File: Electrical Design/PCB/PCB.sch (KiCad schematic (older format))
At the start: 52 parts, among them J1 Conn_02x03_Odd_Even, J2 10118193-0001LF, M1 Camera_Servo, M2 Release_Servo, Q1 LED_MOS, Q2 CAMERA_MOS, Q3 RELEASE_MOS, U1 ADP3338AKCZ-5-R7, U2 BNO080, U3 ADP3338AKCZ-3.3-R7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

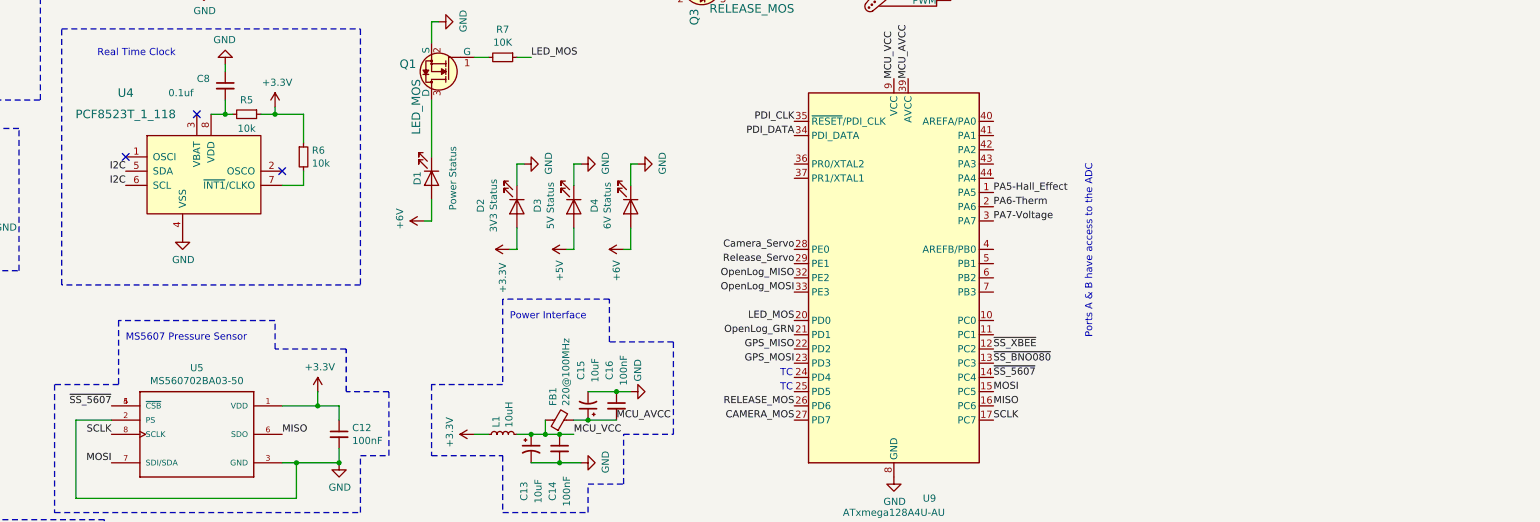
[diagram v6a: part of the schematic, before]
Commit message: Add a lot of libraries and footprints
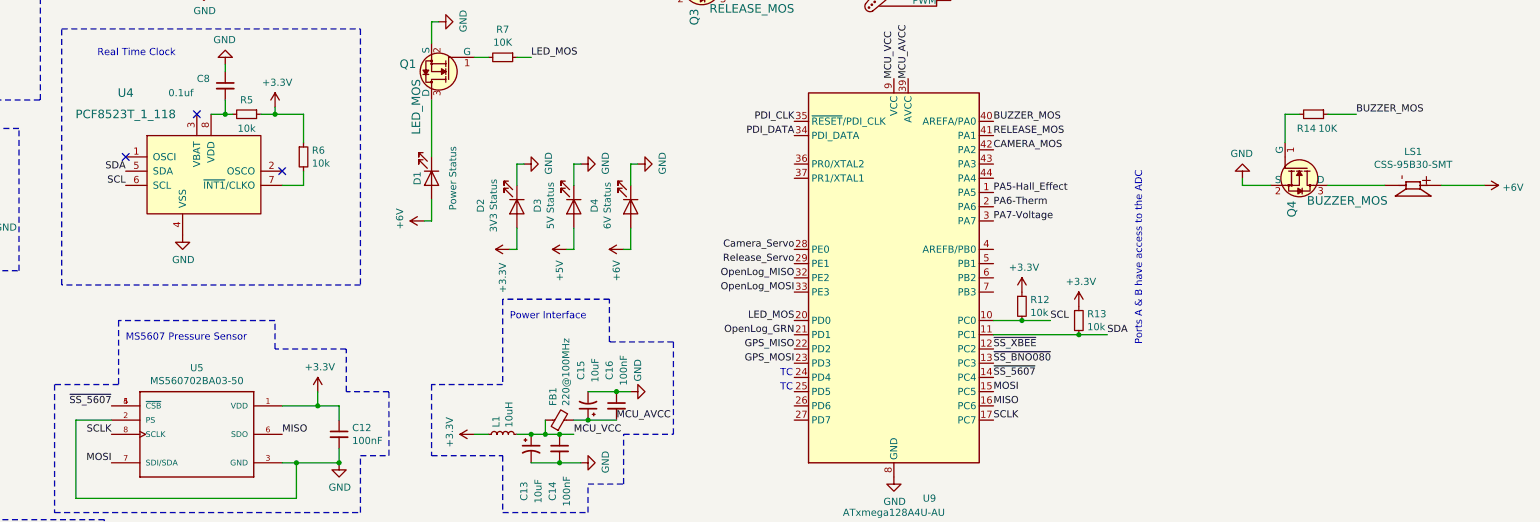
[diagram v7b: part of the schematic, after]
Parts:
- added LS1: CSS-95B30-SMT, CSS-95B30-SMT:CUI_CSS-95B30-SMT, symbol CSS-95B30-SMT:CSS-95B30-SMT
- added Q4: BUZZER_MOS, digikey-footprints:SOT-23-3, symbol dk_Transistors-FETs-MOSFETs-Single:2N7002K-T1-E3
- added R12, R13: 10k, Resistor_SMD:R_0805_2012Metric_Pad1.15x1.40mm_HandSolder, symbol Device:R_Small
- added R14: 10K, Resistor_SMD:R_0805_2012Metric_Pad1.15x1.40mm_HandSolder, symbol Device:R_Small
- J1: footprint (none) -> Connector:Tag-Connect_TC2030-IDC-FP_2x03_P1.27mm_Vertical
- M1, M2: footprint (none) -> Connector_PinHeader_2.54mm:PinHeader_1x03_P2.54mm_Horizontal
- R1, R10, R11, R2, R3, R4, R5, R6, R7, R8, R9: footprint Resistor_SMD:R_0805_2012Metric -> Resistor_SMD:R_0805_2012Metric_Pad1.15x1.40mm_HandSolder
- U1: footprint (none) -> ADP3338AKCZ-5-R7:SOT230P700X180-4N
- U2: footprint (none) -> BNO080:LGA-28
- U3: footprint (none) -> ADP3338AKCZ-3.3RL7:SOT230P700X180-4N
- U5: footprint (none) -> MS560702BA03-50:SON125P300X500X100-8N
- U6: footprint (none) -> Connector_PinHeader_2.00mm:PinHeader_1x03_P2.00mm_Horizontal
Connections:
- net +3V3: now also R12.1, R13.1
- net +6V: now also LS1.P
- net CAMERA_MOS: now also U9.42 (PA2); no longer U9.27 (PD7)
- net GND: now also Q4.2 (S)
- net RELEASE_MOS: now also U9.41 (PA1); no longer U9.26 (PD6)
- net SCL: now reaches U9.10 (PC0)
- net SCL: now also U4.6 (SCL), R12.2
- net SDA: now reaches U9.11 (PC1)
- net SDA: now also U4.5 (SDA), R13.2
- net BUZZER_MOS: now reaches U9.40 (AREFA/PA0)
- net BUZZER_MOS: now also R14.1
- removed net I2C: U4.5 (SDA), U4.6 (SCL)
- new net: LS1.N, Q4.3 (D)
- new net: Q4.1 (G), R14.2

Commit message: Netlist
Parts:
- C13, C15: footprint (none) -> Capacitor_THT:CP_Radial_D10.0mm_P5.00mm
- C2, C3, C5: footprint (none) -> Capacitor_THT:CP_Radial_D5.0mm_P2.00mm
- U7: footprint (none) -> Connectors:1X09
- U8: footprint (none) -> Connectors:1X06
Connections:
- net +3V3: now also U7.8 (VIN)
- net GND: now also U7.7 (GND)
- net GPS_RX: now also U7.6 (RX)
- net GPS_TX: now also U7.5 (TX)
- no-connect marks 7 -> 12
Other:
- moved on the sheet: U7
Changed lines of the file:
@@
 F 0 "C13" V 7050 5550 50  0000 C CNN
 F 1 "10uF" V 7150 5550 50  0000 C CNN
-F 2 "" H 7100 5850 50  0001 C CNN
+F 2 "Capacitor_THT:CP_Radial_D10.0mm_P5.00mm" H 7100 5850 50  0001 C CNN
 F 3 "~" H 7100 5850 50  0001 C CNN
 	1    7100 5850
@@
 F 0 "C15" V 7550 5300 50  0000 C CNN
 F 1 "10uF" V 7450 5300 50  0000 C CNN
-F 2 "" H 7500 5550 50  0001 C CNN
+F 2 "Capacitor_THT:CP_Radial_D10.0mm_P5.00mm" H 7500 5550 50  0001 C CNN
 F 3 "~" H 7500 5550 50  0001 C CNN
 	1    7500 5550
@@
 F 0 "C2" H 1350 1200 50  0000 L CNN
 F 1 "0.1uF" H 1300 1100 50  0000 L CNN
-F 2 "" H 1400 900 50  0001 C CNN
+F 2 "Capacitor_THT:CP_Radial_D5.0mm_P2.00mm" H 1400 900 50  0001 C CNN
 F 3 "~" H 1400 900 50  0001 C CNN
 	1    1400 900
@@
 F 0 "C3" H 1600 1200 50  0000 L CNN
 F 1 "0.1uF" H 1550 1100 50  0000 L CNN
-F 2 "" H 1650 900 50  0001 C CNN
+F 2 "Capacitor_THT:CP_Radial_D5.0mm_P2.00mm" H 1650 900 50  0001 C CNN
 F 3 "~" H 1650 900 50  0001 C CNN
 	1    1650 900
@@
 F 0 "C5" H 2791 2996 50  0000 L CNN
 F 1 "0.1uF" H 2791 2905 50  0000 L CNN
-F 2 "" H 2700 2950 50  0001 C CNN
+F 2 "Capacitor_THT:CP_Radial_D5.0mm_P2.00mm" H 2700 2950 50  0001 C CNN
 F 3 "~" H 2700 2950 50  0001 C CNN
 	1    2700 2950
@@
 L Skyfire_Custom_Components:Adafruit_746 U7
 U 1 1 5C5FC17D
-P 7200 1150
-F 0 "U7" H 6900 1475 50  0000 C CNN
-F 1 "Adafruit_746" H 6900 1384 50  0000 C CNN
-F 2 "" H 7200 1150 50  0001 C CNN
-F 3 "" H 7200 1150 50  0001 C CNN
-	1    7200 1150
-	1    0    0    -1
-$EndComp
-Text Label 7250 1150 0    50   ~ 0
+P 7450 1350
+F 0 "U7" H 6850 1450 50  0000 C CNN
+F 1 "Adafruit_746" H 6850 1350 50  0000 C CNN
+F 2 "Connectors:1X09" H 7450 1350 50  0001 C CNN
+F 3 "" H 7450 1350 50  0001 C CNN
+	1    7450 1350
+	1    0    0    -1
+$EndComp
+Text Label 7200 800  0    50   ~ 0
 GPS_TX
-Text Label 7250 1050 0    50   ~ 0
+Text Label 7200 700  0    50   ~ 0
 GPS_RX
 Text Label 8950 5150 2    50   ~ 0
@@
 L power:+3.3V #PWR033
 U 1 1 5C6096AA
-P 6400 1000
-F 0 "#PWR033" H 6400 850 50  0001 C CNN
-F 1 "+3.3V" H 6415 1173 50  0000 C CNN
-F 2 "" H 6400 1000 50  0001 C CNN
-F 3 "" H 6400 1000 50  0001 C CNN
-	1    6400 1000
+P 6350 650
+F 0 "#PWR033" H 6350 500 50  0001 C CNN
+F 1 "+3.3V" H 6365 823 50  0000 C CNN
+F 2 "" H 6350 650 50  0001 C CNN
+F 3 "" H 6350 650 50  0001 C CNN
+	1    6350 650
 	1    0    0    -1
 $EndComp
@@
 L power:GND #PWR034
 U 1 1 5C609986
-P 6400 1200
-F 0 "#PWR034" H 6400 950 50  0001 C CNN
-F 1 "GND" H 6405 1027 50  0000 C CNN
-F 2 "" H 6400 1200 50  0001 C CNN
-F 3 "" H 6400 1200 50  0001 C CNN
-	1    6400 1200
-	1    0    0    -1
-$EndComp
-Wire Wire Line
-	6400 1000 6400 1050
-Wire Wire Line
-	6400 1050 6550 1050
-Wire Wire Line
-	6400 1200 6400 1150
-Wire Wire Line
-	6400 1150 6550 1150
+P 6350 850
+F 0 "#PWR034" H 6350 600 50  0001 C CNN
+F 1 "GND" H 6355 677 50  0000 C CNN
+F 2 "" H 6350 850 50  0001 C CNN
+F 3 "" H 6350 850 50  0001 C CNN
+	1    6350 850
+	1    0    0    -1
+$EndComp
+Wire Wire Line
+	6350 650  6350 700
+Wire Wire Line
+	6350 700  6500 700
+Wire Wire Line
+	6350 850  6350 800
+Wire Wire Line
+	6350 800  6500 800
 $Comp
 L Skyfire_Custom_Components:Openlog U8
@@
 F 0 "U8" H 6900 2475 50  0000 C CNN
 F 1 "Openlog" H 6900 2384 50  0000 C CNN
-F 2 "" H 7300 2000 50  0001 C CNN
+F 2 "Connectors:1X06" H 7300 2000 50  0001 C CNN
 F 3 "" H 7300 2000 50  0001 C CNN
 	1    7300 2000
@@
 Text Label 10350 3550 0    50   ~ 0
 BUZZER_MOS
+NoConn ~ 7200 900
+NoConn ~ 7200 1000
+NoConn ~ 6500 900
+NoConn ~ 6500 1000
+NoConn ~ 6500 1100
 $EndSCHEMATC
